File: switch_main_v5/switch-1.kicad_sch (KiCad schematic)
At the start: 40 parts, among them U902 SJA1105QELY

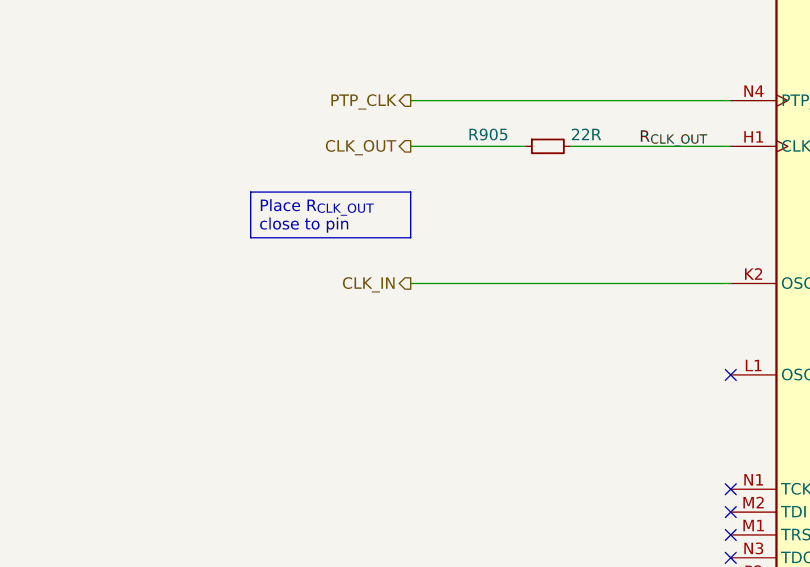
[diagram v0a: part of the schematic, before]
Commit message: MDIO multiplexing
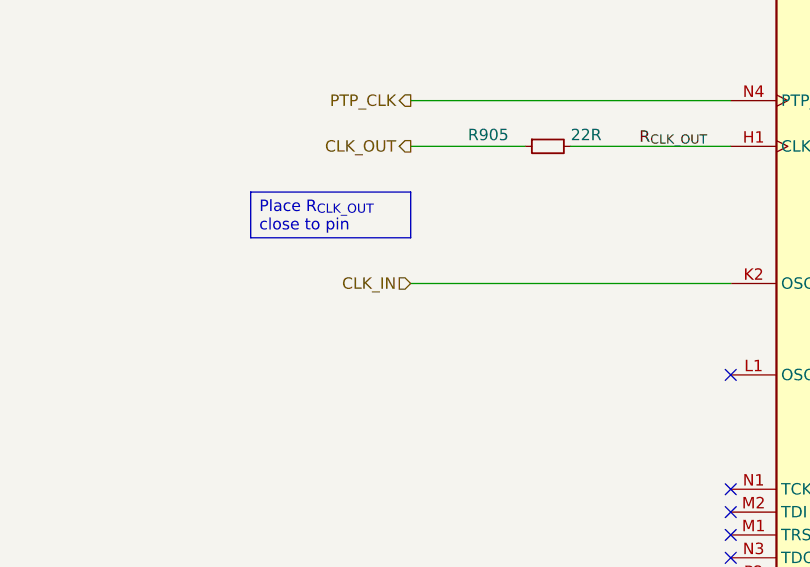
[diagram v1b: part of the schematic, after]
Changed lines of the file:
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@@
 	(title_block
 		(title "Ethernet Switch")
-		(date "2025-06-30")
 		(comment 4 "5 Port gigabit ethernet switch.")
 	)
@@
 	)
 	(hierarchical_label "CLK_IN"
-		(shape output)
+		(shape input)
 		(at 220.98 157.48 180)
 		(effects

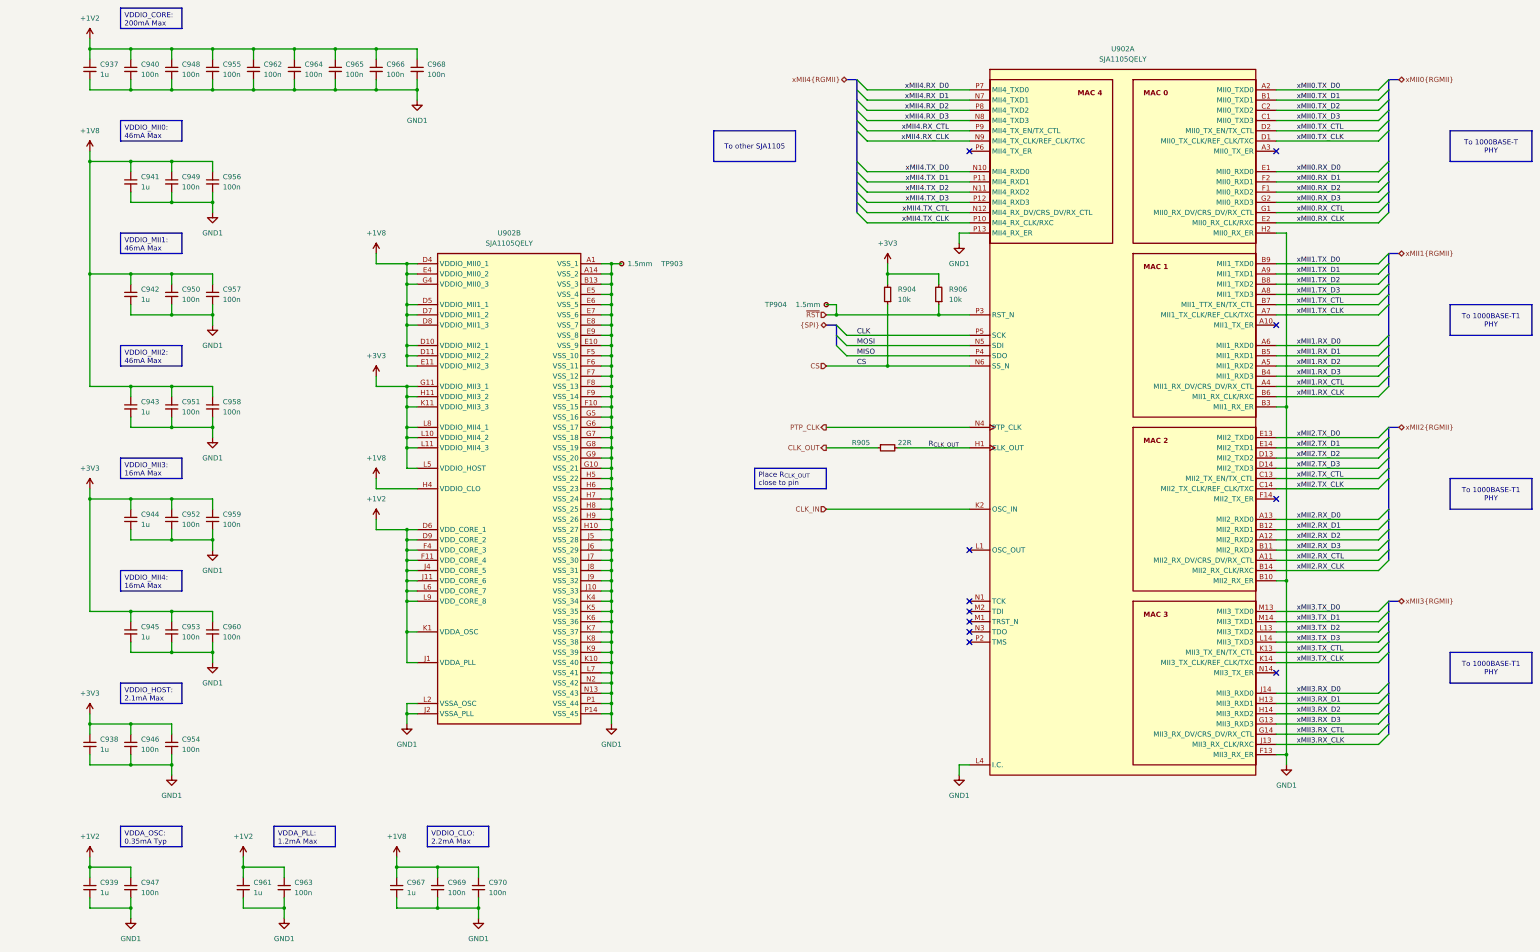
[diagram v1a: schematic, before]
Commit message: Updated 1v0_buck_converter feedback resistors
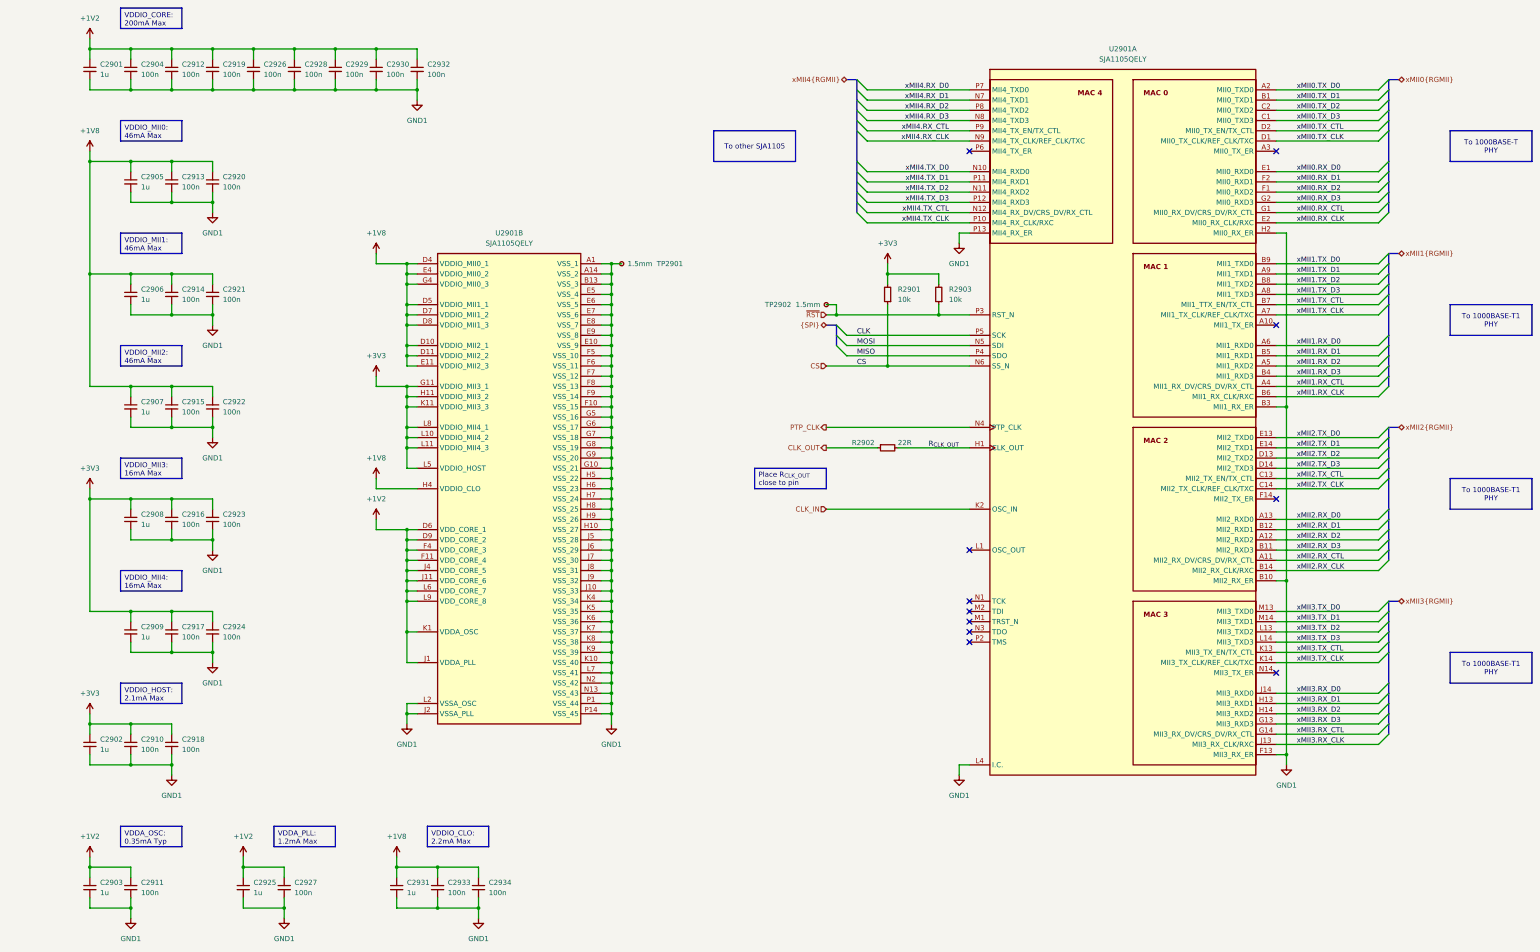
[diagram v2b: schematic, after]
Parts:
- renumbered C937 to C2901, C938 to C2902, C939 to C2903, C940 to C2904, C941 to C2905, C942 to C2906, C943 to C2907, C944 to C2908, C945 to C2909, C946 to C2910, C947 to C2911, C948 to C2912, C949 to C2913, C950 to C2914, C951 to C2915, C952 to C2916, C953 to C2917, C954 to C2918, C955 to C2919, C956 to C2920, C957 to C2921, C958 to C2922, C959 to C2923, C960 to C2924, C961 to C2925, C962 to C2926, C963 to C2927, C964 to C2928, C965 to C2929, C966 to C2930, C967 to C2931, C968 to C2932, C969 to C2933, C970 to C2934, R904 to R2901, R905 to R2902, R906 to R2903, TP903 to TP2901, TP904 to TP2902, U902 to U2901

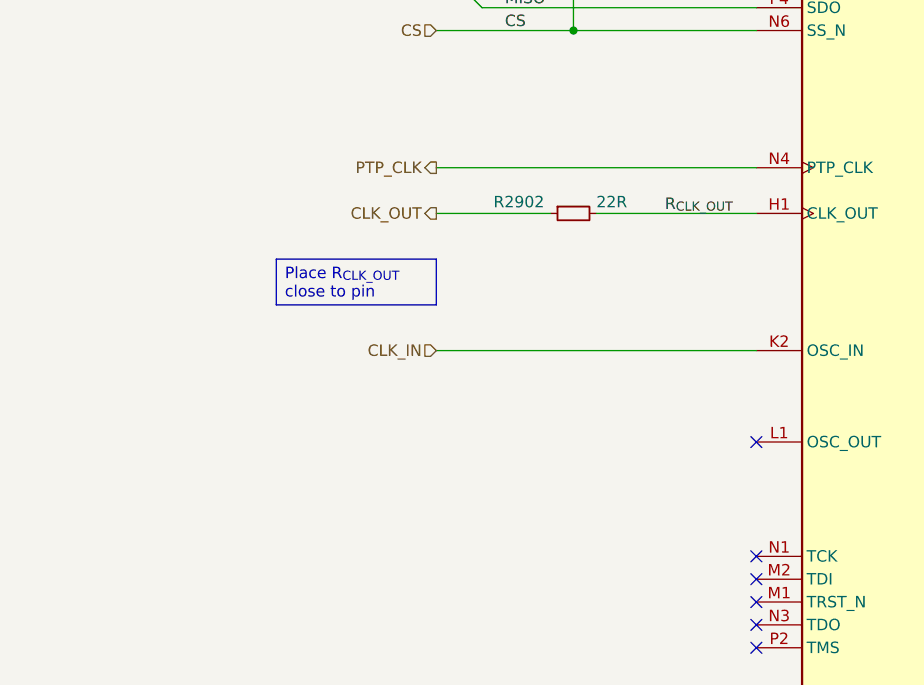
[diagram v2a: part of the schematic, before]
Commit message: Changed main 3V3 regulator to 3A, added switch 2 crystal & other changes
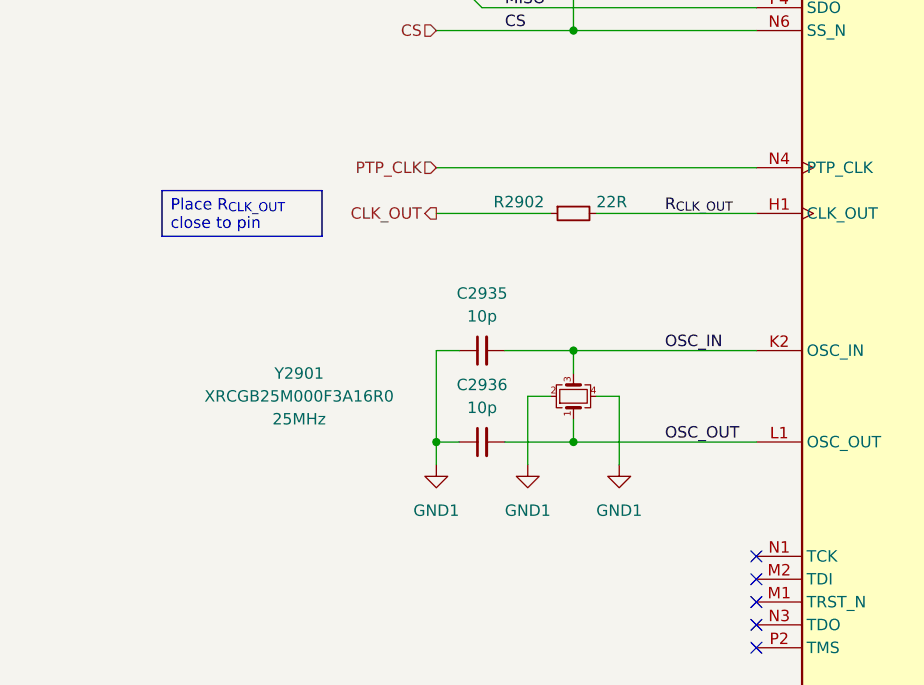
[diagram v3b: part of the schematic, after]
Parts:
- added C2935, C2936: 10p, Capacitor_SMD:C_0402_1005Metric, symbol Device:C_Small
- added Y2901: XRCGB25M000F3A16R0, project_footprints:XRCGB25M000F3A16R0, symbol Device:Crystal_GND24_Small
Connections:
- net GND1: now also C2935.1, C2936.1, Y2901.2, Y2901.4
- net OSC_OUT: now reaches U2901.L1 (OSC_OUT)
- net OSC_OUT: now also C2936.2, Y2901.1
- net CLK_IN renamed OSC_IN
- net OSC_IN: now also C2935.2, Y2901.3
- no-connect marks 11 -> 10

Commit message: Placed most remaining passives and test points
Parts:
- removed TP2902: 1.5mm, TestPoint:TestPoint_Pad_D1.5mm, symbol Connector:TestPoint_Small
- R2903: now not fitted; now left out of the parts list
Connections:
- net CS renamed SS
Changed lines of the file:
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@@
 	)
 	(junction
-		(at 223.52 109.22)
-		(diameter 0)
-		(color 0 0 0 0)
-	)
-	(junction
 		(at 48.26 53.34)
 		(diameter 0)
@@
 	(wire
 		(pts
-			(xy 223.52 109.22) (xy 248.92 109.22)
-		)
-		(stroke
-			(width 0)
-			(type default)
-		)
-	)
-	(wire
-		(pts
 			(xy 116.84 101.6) (xy 119.38 101.6)
 		)
@@
 	(wire
 		(pts
-			(xy 220.98 109.22) (xy 223.52 109.22)
+			(xy 220.98 109.22) (xy 248.92 109.22)
 		)
 		(stroke
@@
 	(wire
 		(pts
-			(xy 223.52 106.68) (xy 223.52 109.22)
-		)
-		(stroke
-			(width 0)
-			(type default)
-		)
-	)
-	(wire
-		(pts
 			(xy 256.54 86.36) (xy 231.14 86.36)
 		)
@@
 	(wire
 		(pts
-			(xy 220.98 106.68) (xy 223.52 106.68)
-		)
-		(stroke
-			(width 0)
-			(type default)
-		)
-	)
-	(wire
-		(pts
 			(xy 167.64 152.4) (xy 167.64 154.94)
 		)
@@
 		)
 	)
-	(label "CS"
-		(at 228.6 121.92 0)
-		(effects
-			(font
-				(size 1.27 1.27)
-			)
-			(justify left bottom)
-		)
-	)
 	(label "xMII3.RX_D1"
 		(at 337.82 205.74 0)
@@
 		)
 	)
-	(hierarchical_label "CS"
+	(hierarchical_label "SS"
 		(shape input)
 		(at 220.98 121.92 180)
@@
 		(unit 1)
 		(exclude_from_sim no)
-		(in_bom yes)
-		(on_board yes)
-		(dnp no)
+		(in_bom no)
+		(on_board no)
+		(dnp yes)
 		(fields_autoplaced yes)
 		(property "Reference" "R2903"
@@
 					(unit 1)
 				)
-			)
-		)
-	)
-	(symbol
-		(lib_id "Connector:TestPoint_Small")
-		(at 220.98 106.68 0)
-		(mirror y)
-		(unit 1)
-		(exclude_from_sim no)
-		(in_bom no)
-		(on_board yes)
-		(dnp no)
-		(property "Reference" "TP2902"
-			(at 205.74 106.68 0)
-			(effects
-				(font
-					(size 1.27 1.27)
-				)
-				(justify right)
-			)
-		)
-		(property "Value" "1.5mm"
-			(at 213.36 106.68 0)
-			(effects
-				(font
-					(size 1.27 1.27)
-				)
-				(justify right)
-			)
-		)
-		(property "Footprint" "TestPoint:TestPoint_Pad_D1.5mm"
-			(at 215.9 106.68 0)
-			(effects
-				(font
-					(size 1.27 1.27)
-				)
-				(hide yes)
-			)
-		)
-		(property "Datasheet" "~"
-			(at 215.9 106.68 0)
-			(effects
-				(font
-					(size 1.27 1.27)
-				)
-				(hide yes)
-			)
-		)
-		(property "Description" "test point"
-			(at 220.98 106.68 0)
-			(effects
-				(font
-					(size 1.27 1.27)
-				)
-				(hide yes)
-			)
-		)
-		(pin "1"
-		)
-		(instances
-			(project "switch_main_v5"
-				(path "/a5e57332-4284-4d3c-ab3c-13bc0ddb29b6/31c4512b-1e39-4437-8559-238fb7009a56"
-					(reference "TP2902")
-					(unit 1)
-				)

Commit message: Tidied schematic and PCB
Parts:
- renumbered C2901 to C1601, C2904 to C1602, C2912 to C1603, C2919 to C1604, C2926 to C1605, C2928 to C1606, C2929 to C1607, C2930 to C1608, C2932 to C1609, C2905 to C1610, C2913 to C1611, C2920 to C1612, C2906 to C1613, C2914 to C1614, C2921 to C1615, C2907 to C1616, C2915 to C1617, C2922 to C1618, C2935 to C1619, C2908 to C1620, C2916 to C1621, C2923 to C1622, C2936 to C1623, C2909 to C1624, C2917 to C1625, C2924 to C1626, C2902 to C1627, C2910 to C1628, C2918 to C1629, C2903 to C1630, C2911 to C1631, C2925 to C1632, C2927 to C1633, C2931 to C1634, C2933 to C1635, C2934 to C1636, R2901 to R1601, R2903 to R1602, R2902 to R1603, TP2901 to TP1601, U2901 to U1601, Y2901 to Y1601
